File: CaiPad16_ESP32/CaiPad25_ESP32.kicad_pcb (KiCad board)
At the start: 2 copper layers, 117.9 x 88.3 mm, 34 parts, among them U1 ESP32_DevKit_V1_DOIT, U2 NRF24L01_Breakout

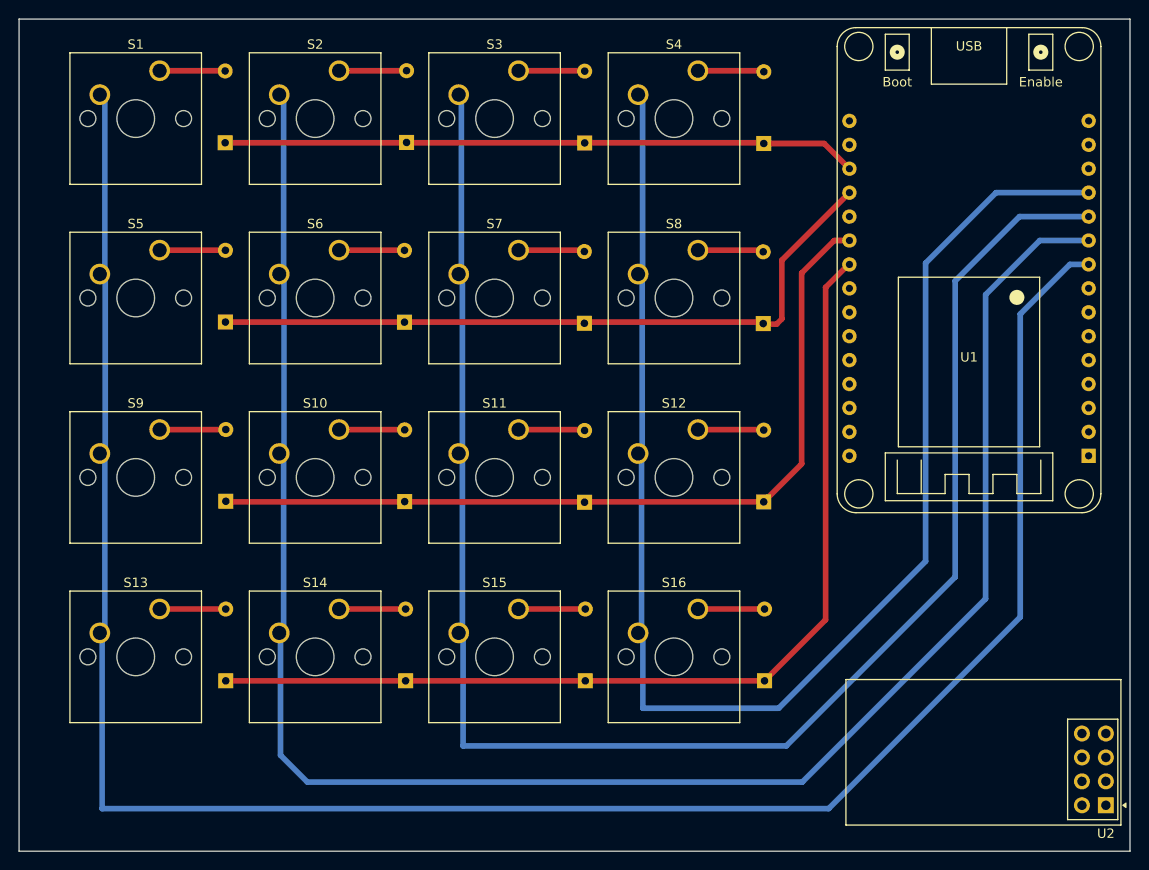
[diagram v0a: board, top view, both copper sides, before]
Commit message: added pro micro firmware
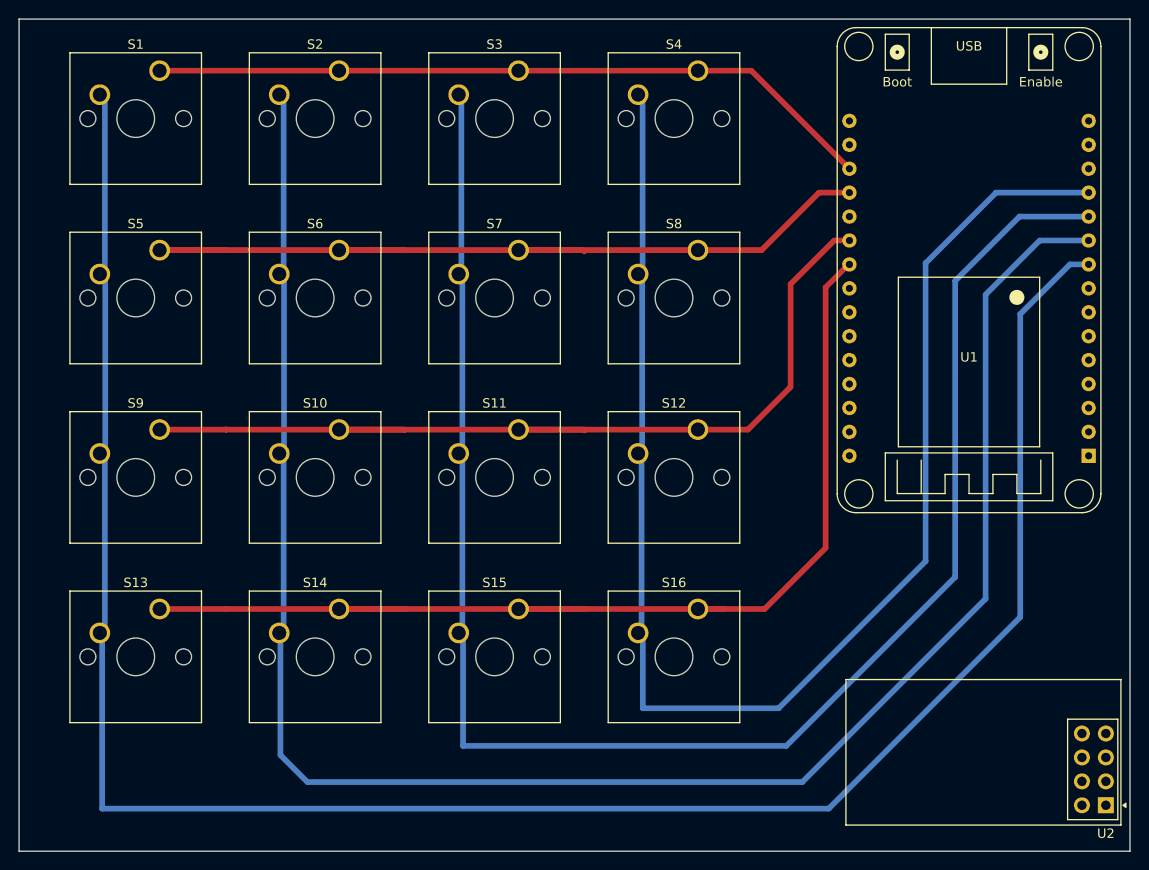
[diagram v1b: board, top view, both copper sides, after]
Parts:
- removed D1, D10, D11, D12, D13, D14, D15, D16, D2, D3, D4, D5, D6, D7, D8, D9: Diode, ScottoKeebs_Components:Diode_DO-35
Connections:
- S1 pad 1: Net-(D1-A) -> Row 0
- S10 pad 1: Net-(D10-A) -> Row 2
- S11 pad 1: Net-(D11-A) -> Row 2
- S12 pad 1: Net-(D12-A) -> Row 2
- S13 pad 1: Net-(D13-A) -> Row 3
- S14 pad 1: Net-(D14-A) -> Row 3
- S15 pad 1: Net-(D15-A) -> Row 3
- S16 pad 1: Net-(D16-A) -> Row 3
- S2 pad 1: Net-(D2-A) -> Row 0
- S3 pad 1: Net-(D3-A) -> Row 0
- S4 pad 1: Net-(D4-A) -> Row 0
- S5 pad 1: Net-(D5-A) -> Row 1
- S6 pad 1: Net-(D6-A) -> Row 1
- S7 pad 1: Net-(D7-A) -> Row 1
- S8 pad 1: Net-(D8-A) -> Row 1
- S9 pad 1: Net-(D9-A) -> Row 2
- U1 pad 12: Column 3 -> unconnected-(U1-IO12-Pad12)
- U1 pad 13: unconnected-(U1-IO13-Pad13) -> Column 3
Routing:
- net Row 1: track 75.8 -> 96.8 mm
- net Row 3: track 105.2 -> 121.6 mm
- net Row 2: track 89.6 -> 102.0 mm
- net Row 0: track 67.4 -> 77.5 mm
- net Net-(D2-A): track 7.17 -> 0.00 mm
- net Net-(D15-A): track 7.10 -> 0.00 mm
- net Net-(D16-A): track 7.08 -> 0.00 mm
- net Net-(D14-A): track 7.07 -> 0.00 mm
- net Net-(D7-A): track 7.06 -> 0.00 mm
- net Net-(D11-A): track 7.05 -> 0.00 mm
- net Net-(D3-A): track 7.04 -> 0.00 mm
- net Net-(D4-A): track 7.04 -> 0.00 mm
- net Net-(D9-A): track 7.03 -> 0.00 mm
- net Net-(D13-A): track 7.02 -> 0.00 mm
- net Net-(D12-A): track 7.01 -> 0.00 mm
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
